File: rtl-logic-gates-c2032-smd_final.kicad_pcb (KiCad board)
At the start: 2 copper layers, 74 x 55 mm, 61 parts, among them Q1 AO3401A, Q10 MMBT3904, Q11 MMBT3904, Q12 MMBT3904, Q13 MMBT3904, Q14 MMBT3904, Q2 MMBT3904, Q3 MMBT3904, Q4 MMBT3904, Q5 MMBT3904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

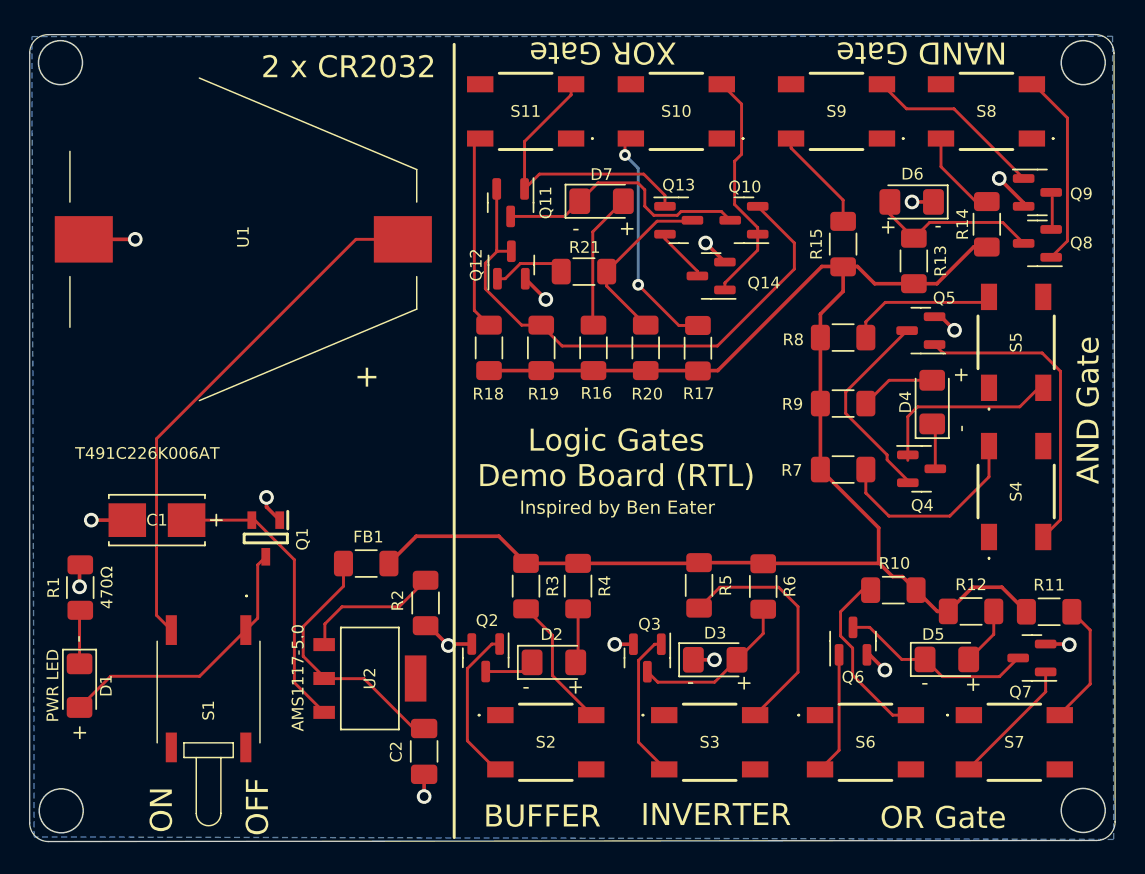
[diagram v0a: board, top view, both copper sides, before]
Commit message: Saved with Kicad v8 and fixed footprints to clear all DRC errors/warnings
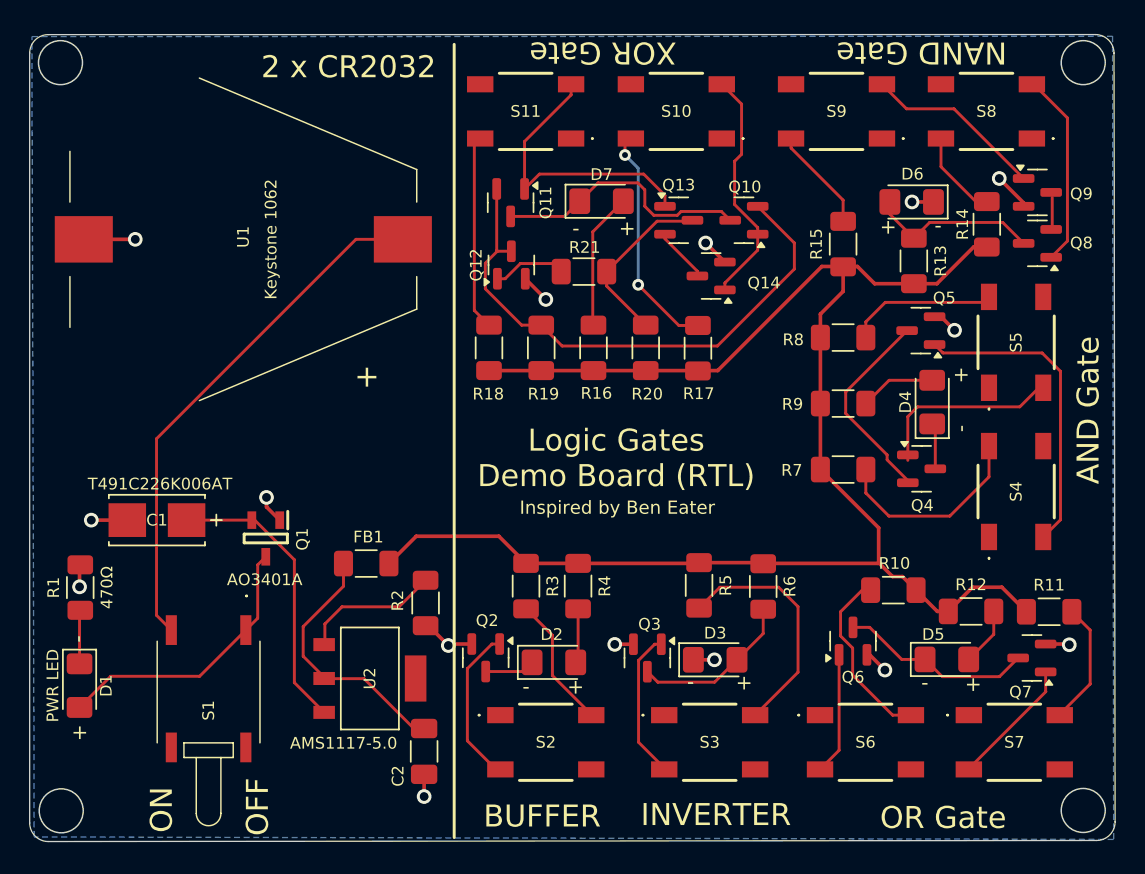
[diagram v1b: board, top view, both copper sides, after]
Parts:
- G1: footprint lutzcraft:Lutzcraft_logo_1125DPI -> logic_gates_footprints:Lutzcraft_logo_1125DPI

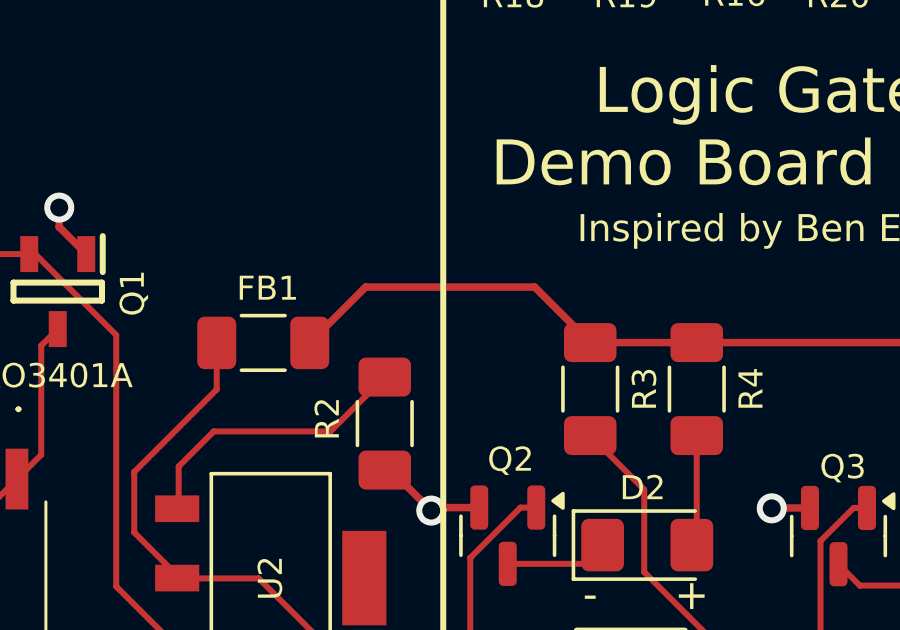
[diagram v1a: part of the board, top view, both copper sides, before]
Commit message: Upgraded project to KiCad 9.0.3.
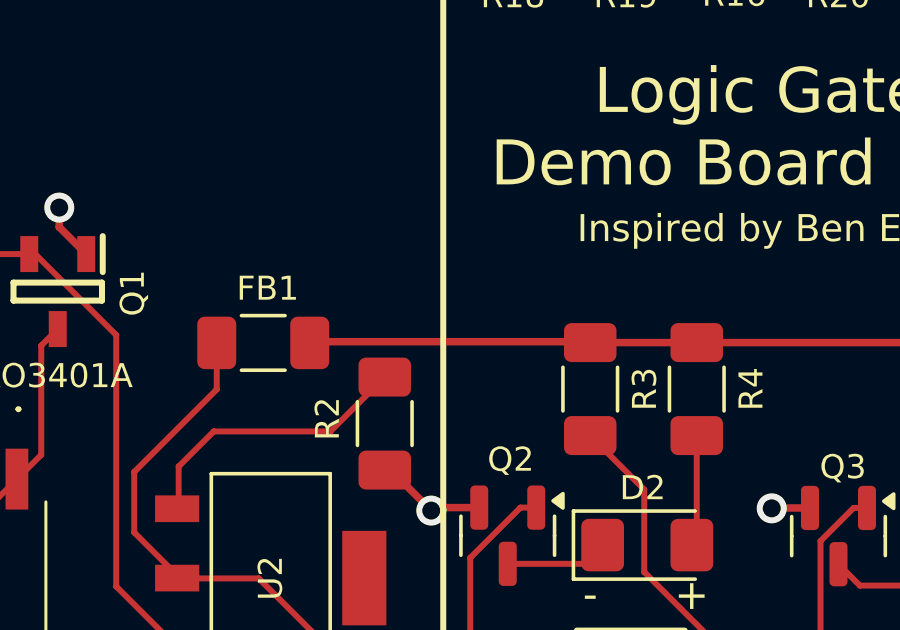
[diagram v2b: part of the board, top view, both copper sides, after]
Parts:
- removed REF1: OSHW-Logo_7.5x8mm_SilkScreen, Symbol:OSHW-Logo_7.5x8mm_SilkScreen
- added REF**: OSHW-Logo_7.5x8mm_SilkScreen, Symbol:OSHW-Logo_7.5x8mm_SilkScreen, B.Cu at (136.6, 108.8)
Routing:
- net 5V: track 108.7 -> 107.2 mm
